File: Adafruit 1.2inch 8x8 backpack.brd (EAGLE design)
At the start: 40.6 x 32 mm, 16 parts, among them CN1 1X4-CLEANBIG

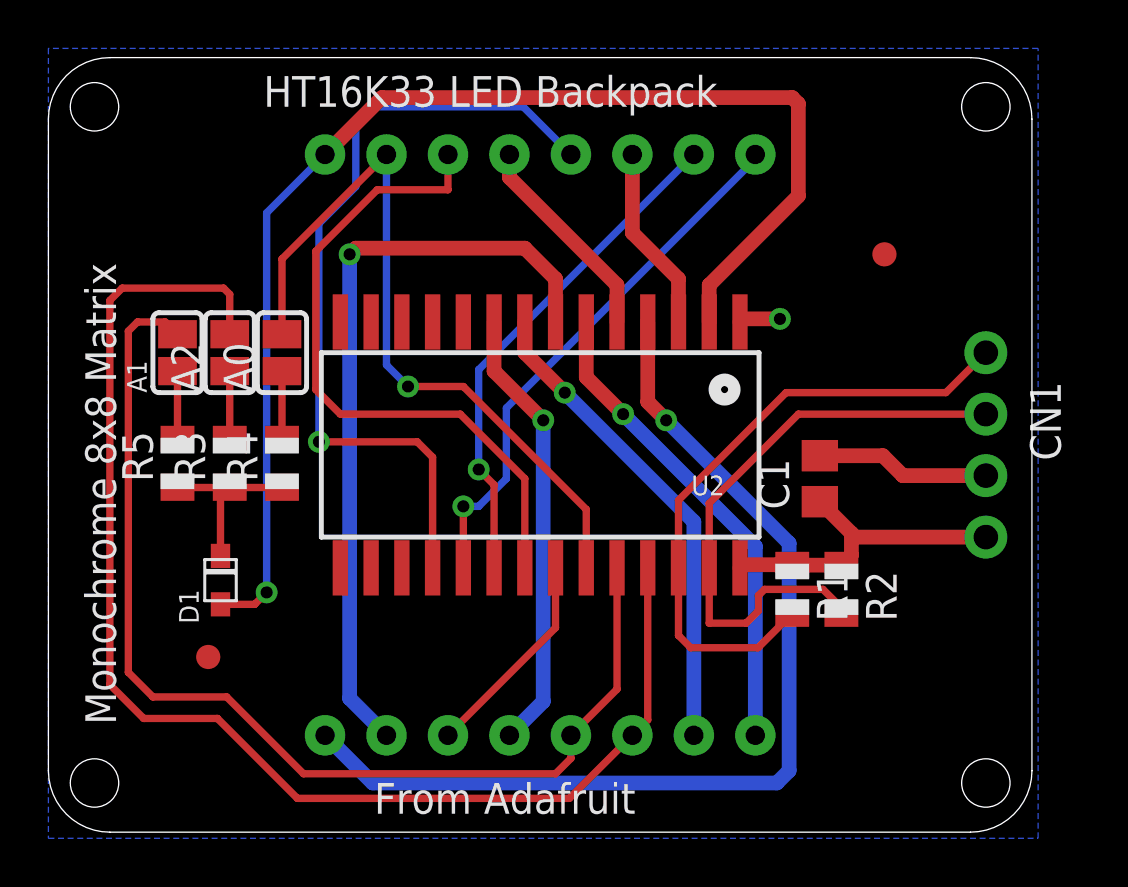
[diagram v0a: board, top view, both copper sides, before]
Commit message: Update 1.2-inch 8x8 backpack files
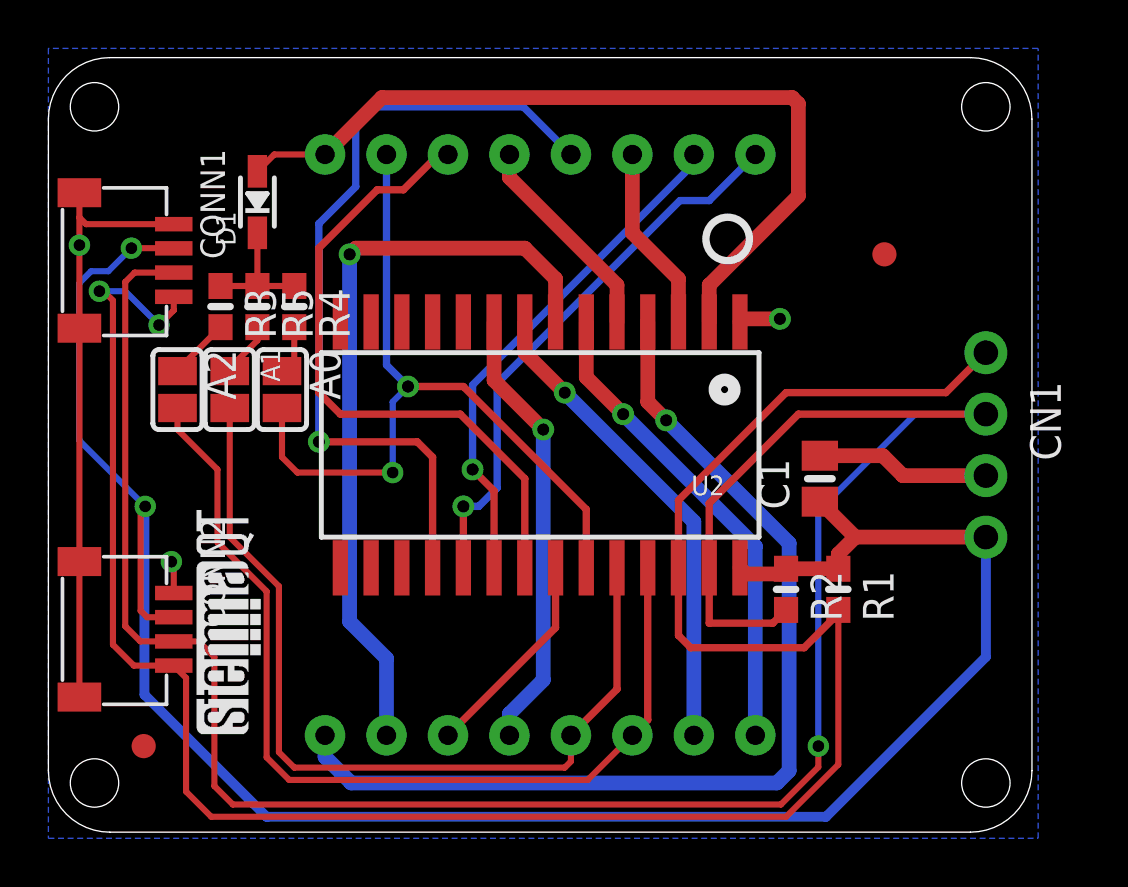
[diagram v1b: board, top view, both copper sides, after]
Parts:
- added CONN1, CONN2: STEMMA_I2C_QT, adafruit_electromech:JST_SH4
- added PLABEL0: (no value), pinguin:PLABEL0
- added PLABEL1: (no value), pinguin:PLABEL1
- added PLABEL10: (no value), pinguin:PLABEL10
- added PLABEL11: (no value), pinguin:PLABEL11
- added PLABEL12: (no value), pinguin:PLABEL12
- added PLABEL13: (no value), pinguin:PLABEL13
- added PLABEL2: (no value), pinguin:PLABEL2
- added PLABEL3: (no value), pinguin:PLABEL3
- added PLABEL4: (no value), pinguin:PLABEL4
- added PLABEL5: (no value), pinguin:PLABEL5
- added PLABEL6: (no value), pinguin:PLABEL6
- added PLABEL7: (no value), pinguin:PLABEL7
- added PLABEL8: (no value), pinguin:PLABEL8
- added PLABEL9: (no value), pinguin:PLABEL9
- added U$4: (no value), microbuilder:PCBFEAT-REV-040
- added U$5: (no value), silks:STEMMAQT
- C1: device rcl:C0805 -> microbuilder:0805-NO
- D1: device adafruit:SOD-323F -> microbuilder:SOD-323
- LED1: device microbuilder:SEGMENT_BL-M12A881UR -> adafruit_display:SEGMENT_BL-M12A881UR
- R1, R2, R3, R4, R5: device adafruit:R0805 -> microbuilder:0603-NO
- U2: value (none) -> HT16K33; device microbuilder:SOP28_300MIL -> adafruit_display:SOP28_300MIL
- moved D1 15.7 mm to (-11.7, 10.0)
- moved R5 7.27 mm to (-11.7, 5.71), turned to 270 degrees
- moved R4 6.50 mm to (-10.2, 5.71), turned to 270 degrees
- moved R3 6.49 mm to (-13.2, 5.71), turned to 270 degrees
- moved U$1 4.55 mm to (-16.4, -12.4)
- moved A1 2.64 mm to (-12.8, 2.29), turned to 270 degrees
- moved A2 2.64 mm to (-15.0, 2.29), turned to 270 degrees
- moved R2 2.29 mm to (10.2, -5.97)
- moved R1 1.91 mm to (12.3, -5.97)
- moved A0 1.52 mm to (-10.7, 2.29), turned to 270 degrees
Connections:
- net GND: now also CONN1.1, CONN1.MT1, CONN1.MT2, CONN2.1, CONN2.MT1, CONN2.MT2
- net SCL: now also CONN1.4, CONN2.4
- net SDA: now also CONN1.3, CONN2.3
- net VDD: now also CONN1.2, CONN2.2
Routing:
- net VDD: track 13.2 -> 86.4 mm, vias 0 -> 2
- net SDA: track 24.9 -> 92.3 mm, vias 0 -> 1
- net SCL: track 26.3 -> 90.6 mm, vias 0 -> 2
- net GND: track 8.90 -> 35.1 mm, vias 1 -> 3
- net N$8: track 52.4 -> 34.3 mm, vias 1 -> 0
- net A2: track 54.6 -> 39.4 mm
- net A1: track 45.4 -> 36.3 mm
- net N$14: track 7.53 -> 5.25 mm
- net A0: track 31.1 -> 32.5 mm, vias 1 -> 2
- net N$13: track 27.5 -> 26.6 mm
- net N$20: track 2.81 -> 2.03 mm
- net SEG_G: track 22.4 -> 23.2 mm
- net N$6: track 41.2 -> 41.7 mm
- net N$10: track 2.81 -> 2.29 mm
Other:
- board text added: "from adafruit!"
- board text removed: "From Adafruit"
